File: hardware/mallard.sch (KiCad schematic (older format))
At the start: 84 parts, among them J1 USB_A, J2 Conn_02x03_Odd_Even, J3 Conn_01x03, J4 Conn_01x03, J5 Conn_01x03, J6 Conn_01x03, SW1 RESET Switch, U1 TMP235, U10 LTC1983ES6-3, U11 STM32L4Q5xx, U12 LTC3529EDCB, U2 TMP235, U3 TMP235, U4 BQ24210DQCT, U5 TMUX1309, U6 TMUX1309, U7 LMP7721, U8 TPS71710DRVR, U9 LMV554

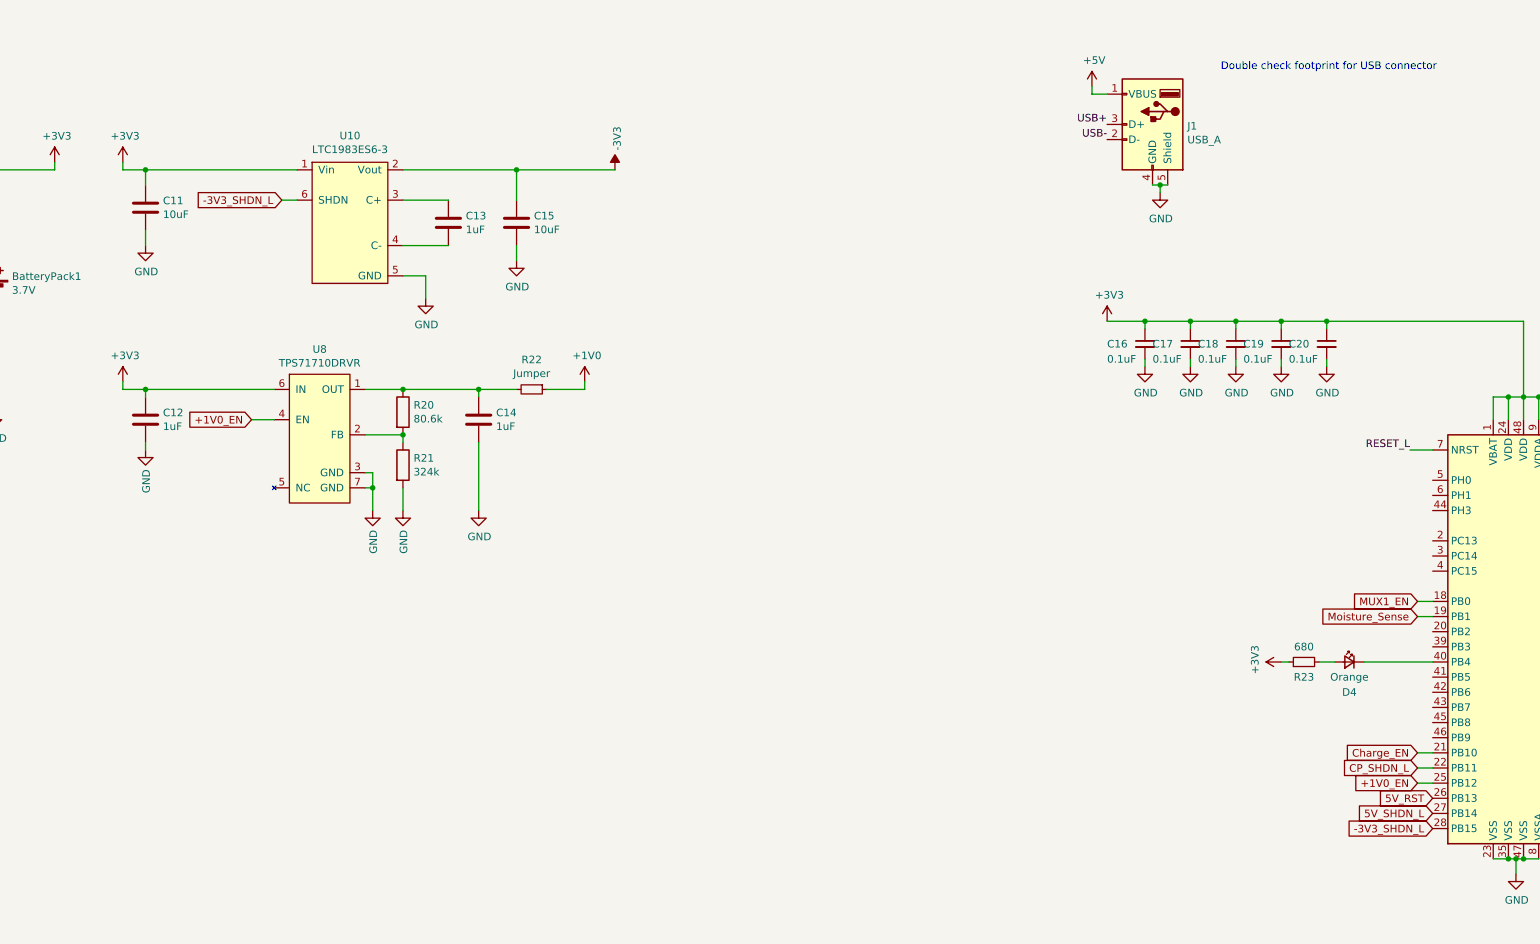
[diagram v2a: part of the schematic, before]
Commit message: Replaced -3V charge pump with LM828
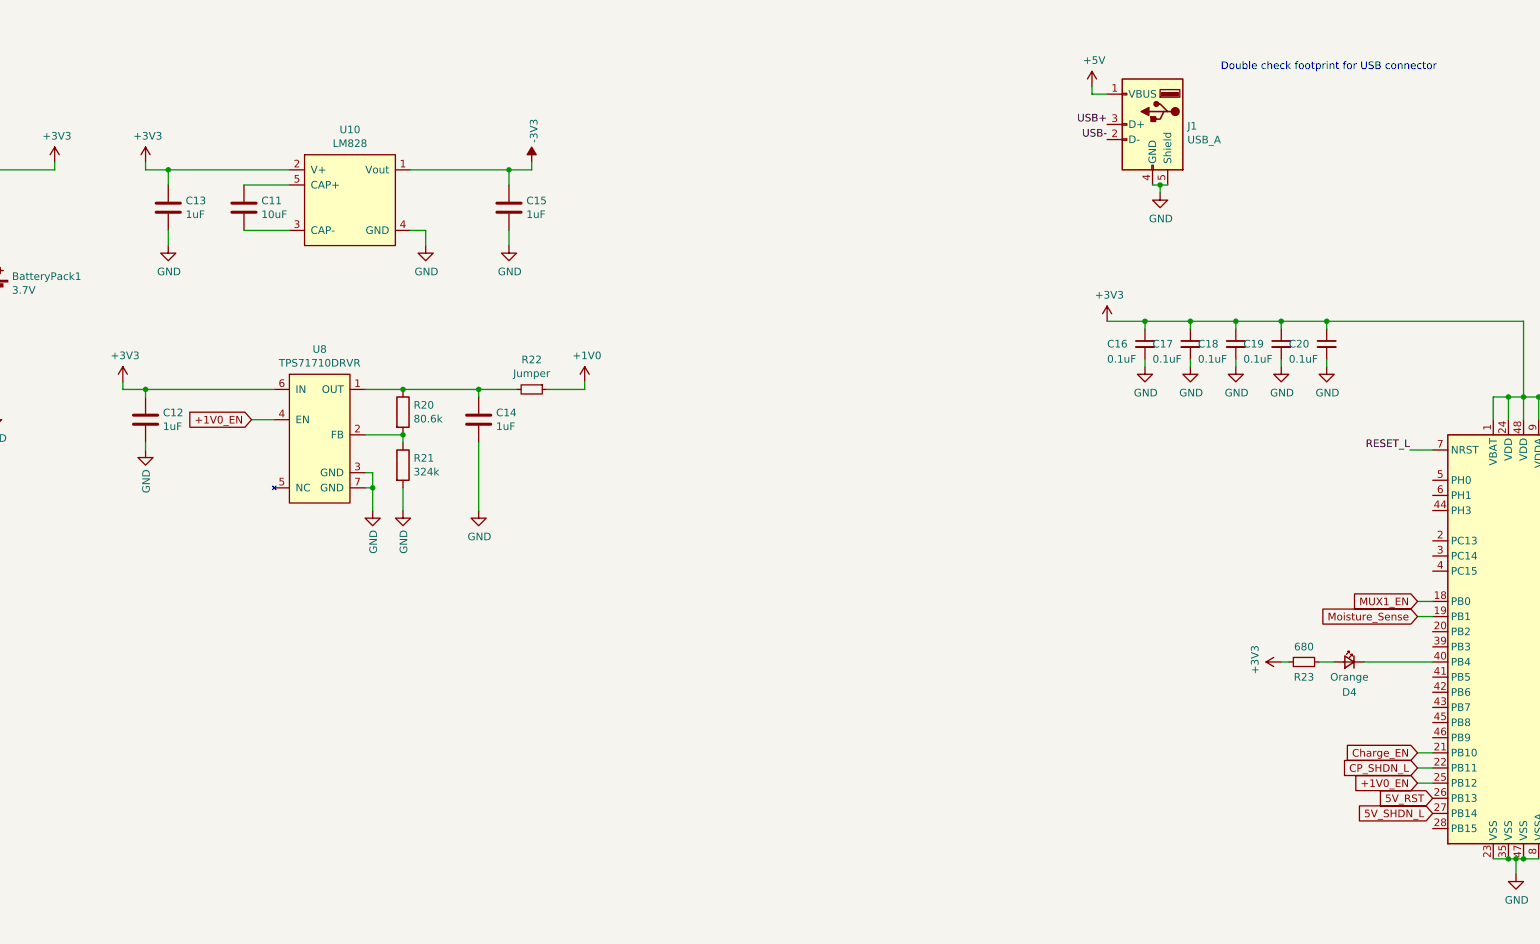
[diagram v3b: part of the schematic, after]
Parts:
- removed U10: LTC1983ES6-3, Package_TO_SOT_SMD:SOT-23-6, symbol mallard-rescue:LTC1983ES6-3-mallard
- added U10: LM828, Package_TO_SOT_SMD:SOT-23-5, symbol mallard:LM828
- C13: Digikey 1276-1019-1-ND -> 311-1446-1-ND
- C15: value 10uF -> 1uF; Digikey 587-3258-1-ND -> 311-1446-1-ND
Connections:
- net +3V3: now also C13.1, U10.2 (V+); no longer C11.1
- net -3V3: now also U10.1 (Vout)
- net GND: now also C13.2, U10.4 (GND); no longer C11.2
- net -3V3_SHDN_L: no longer names the net of U11.28 (PB15)
- new net: C11.2, U10.3 (CAP-)
- new net: C11.1, U10.5 (CAP+)
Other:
- moved on the sheet: C11
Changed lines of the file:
@@
 	1700 10800 1700 10900
-Wire Wire Line
-	9650 3200 9950 3200
-Wire Wire Line
-	9650 3500 9950 3500
 Wire Wire Line
 	3050 3950 2950 3950
@@
 F 3 "" H 2450 4600 50  0001 C CNN
 	1    2450 4600
-	1    0    0    -1
-$EndComp
-$Comp
-L mallard-rescue:GND-power #PWR0149
-U 1 1 62037076
-P 9800 3850
-F 0 "#PWR0149" H 9800 3600 50  0001 C CNN
-F 1 "GND" H 9805 3677 50  0000 C CNN
-F 2 "" H 9800 3850 50  0001 C CNN
-F 3 "" H 9800 3850 50  0001 C CNN
-	1    9800 3850
 	1    0    0    -1
 $EndComp
@@
 Wire Wire Line
 	6950 3000 7350 3000
-$Comp
-L mallard-rescue:GND-power #PWR0154
-U 1 1 620370B8
-P 7950 3500
-F 0 "#PWR0154" H 7950 3250 50  0001 C CNN
-F 1 "GND" H 7955 3327 50  0000 C CNN
-F 2 "" H 7950 3500 50  0001 C CNN
-F 3 "" H 7950 3500 50  0001 C CNN
-	1    7950 3500
-	1    0    0    -1
-$EndComp
-Wire Wire Line
-	7950 3400 7950 3500
 Wire Wire Line
 	1450 3000 1000 3000
@@
 L mallard-rescue:C-Device C11
 U 1 1 620370D8
-P 7950 3250
-F 0 "C11" H 8065 3296 50  0000 L CNN
-F 1 "10uF" H 8065 3205 50  0000 L CNN
-F 2 "Capacitor_SMD:C_0603_1608Metric_Pad1.08x0.95mm_HandSolder" H 7988 3100 50  0001 C CNN
-F 3 "https://www.yuden.co.jp/productdata/catalog/mlcc06_e.pdf" H 7950 3250 50  0001 C CNN
-F 4 "587-3258-1-ND" H 7950 3250 50  0001 C CNN "Digikey"
-	1    7950 3250
-	1    0    0    -1
-$EndComp
-$Comp
-L mallard-rescue:C-Device C13
-U 1 1 620370DF
-P 9950 3350
-F 0 "C13" H 10065 3396 50  0000 L CNN
-F 1 "1uF" H 10065 3305 50  0000 L CNN
-F 2 "Capacitor_SMD:C_0603_1608Metric_Pad1.08x0.95mm_HandSolder" H 9988 3200 50  0001 C CNN
-F 3 "http://weblib.samsungsem.com/mlcc/mlcc-ec-data-sheet.do?partNumber=CL10B105KO8NNN" H 9950 3350 50  0001 C CNN
-F 4 "1276-1019-1-ND" H 9950 3350 50  0001 C CNN "Digikey"
-	1    9950 3350
+P 8600 3250
+F 0 "C11" H 8715 3296 50  0000 L CNN
+F 1 "10uF" H 8715 3205 50  0000 L CNN
+F 2 "Capacitor_SMD:C_0603_1608Metric_Pad1.08x0.95mm_HandSolder" H 8638 3100 50  0001 C CNN
+F 3 "https://www.yuden.co.jp/productdata/catalog/mlcc06_e.pdf" H 8600 3250 50  0001 C CNN
+F 4 "587-3258-1-ND" H 8600 3250 50  0001 C CNN "Digikey"
+	1    8600 3250
 	1    0    0    -1
 $EndComp
@@
 F 4 "296-28738-1-ND" H 3550 2900 50  0001 C CNN "Digikey"
 	1    3550 2900
-	1    0    0    -1
-$EndComp
-$Comp
-L mallard-rescue:LTC1983ES6-3-mallard U10
-U 1 1 620370FA
-P 9300 2900
-F 0 "U10" H 9300 3025 50  0000 C CNN
-F 1 "LTC1983ES6-3" H 9300 2934 50  0000 C CNN
-F 2 "Package_TO_SOT_SMD:SOT-23-6" H 9300 1850 50  0001 C CNN
-F 3 "https://www.analog.com/media/en/technical-documentation/data-sheets/1983fc.pdf" H 9300 2900 50  0001 C CNN
-F 4 "LTC1983ES6-3#TRPBFCT-ND" H 9300 2900 50  0001 C CNN "Digikey"
-	1    9300 2900
 	1    0    0    -1
 $EndComp
@@
 	-1   0    0    1
 $EndComp
-Text GLabel 8850 3200 0    50   Input ~ 0
--3V3_SHDN_L
-Wire Wire Line
-	8950 3200 8850 3200
-$Comp
-L mallard-rescue:-3V3-power #PWR0156
-U 1 1 62037111
-P 11050 3000
-F 0 "#PWR0156" H 11050 3100 50  0001 C CNN
-F 1 "-3V3" V 11065 3128 50  0000 L CNN
-F 2 "" H 11050 3000 50  0001 C CNN
-F 3 "" H 11050 3000 50  0001 C CNN
-	1    11050 3000
-	1    0    0    -1
-$EndComp
 $Comp
 L mallard-rescue:GND-power #PWR0157
@@
 Wire Wire Line
 	7350 3000 7350 2950
-$Comp
-L mallard-rescue:+3V3-power #PWR0162
-U 1 1 6203717F
-P 7800 2950
-F 0 "#PWR0162" H 7800 2800 50  0001 C CNN
-F 1 "+3V3" H 7815 3123 50  0000 C CNN
-F 2 "" H 7800 2950 50  0001 C CNN
-F 3 "" H 7800 2950 50  0001 C CNN
-	1    7800 2950
-	1    0    0    -1
-$EndComp
-Wire Wire Line
-	7950 3000 7950 3100
-Wire Wire Line
-	7950 3000 8950 3000
-Wire Wire Line
-	7950 3000 7800 3000
-Wire Wire Line
-	7800 3000 7800 2950
-Connection ~ 7950 3000
-Wire Wire Line
-	9650 3000 10400 3000
-$Comp
-L mallard-rescue:GND-power #PWR0163
-U 1 1 6203718B
-P 10400 3600
-F 0 "#PWR0163" H 10400 3350 50  0001 C CNN
-F 1 "GND" H 10405 3427 50  0000 C CNN
-F 2 "" H 10400 3600 50  0001 C CNN
-F 3 "" H 10400 3600 50  0001 C CNN
-	1    10400 3600
-	1    0    0    -1
-$EndComp
-Wire Wire Line
-	10400 3500 10400 3600
-$Comp
-L mallard-rescue:C-Device C15
-U 1 1 62037193
-P 10400 3350
-F 0 "C15" H 10515 3396 50  0000 L CNN
-F 1 "10uF" H 10515 3305 50  0000 L CNN
-F 2 "Capacitor_SMD:C_0603_1608Metric_Pad1.08x0.95mm_HandSolder" H 10438 3200 50  0001 C CNN
-F 3 "https://www.yuden.co.jp/productdata/catalog/mlcc06_e.pdf" H 10400 3350 50  0001 C CNN
-F 4 "587-3258-1-ND" H 10400 3350 50  0001 C CNN "Digikey"
-	1    10400 3350
-	1    0    0    -1
-$EndComp
-Wire Wire Line
-	10400 3000 10400 3200
-Connection ~ 10400 3000
-Wire Wire Line
-	10400 3000 11050 3000
-Wire Wire Line
-	9650 3700 9800 3700
-Wire Wire Line
-	9800 3700 9800 3850
 $Comp
 L mallard-rescue:C-Device C4
@@
 Text GLabel 16450 7150 0    50   Input ~ 0
 5V_RST
-Text GLabel 16450 7350 0    50   Input ~ 0
--3V3_SHDN_L
 Wire Wire Line
 	3200 6300 3600 6300
@@
 	3200 6650 3600 6650
 Connection ~ 3600 6650
+$Comp
+L mallard:LM828 U10
+U 1 1 61F55449
+P 9300 2850
+F 0 "U10" H 9300 2965 50  0000 C CNN
+F 1 "LM828" H 9300 2874 50  0000 C CNN
+F 2 "Package_TO_SOT_SMD:SOT-23-5" H 9300 2000 50  0001 C CNN
+F 3 "https://www.ti.com/lit/ds/symlink/lm828.pdf?HQS=dis-dk-null-digikeymode-dsf-pf-null-wwe&ts=1643222784613&ref_url=https%253A%252F%252Fwww.ti.com%252Fgeneral%252Fdocs%252Fsuppproductinfo.tsp%253FdistId%253D10%2526gotoUrl%253Dhttps%253A%252F%252Fwww.ti.com%252Flit%252Fgpn%252Flm828" H 9300 2850 50  0001 C CNN
+F 4 "296-36289-1-ND" H 9300 2100 50  0001 C CNN "Digikey"
+	1    9300 2850
+	1    0    0    -1
+$EndComp
+Wire Wire Line
+	8600 3100 8900 3100
+Wire Wire Line
+	8600 3400 8900 3400
+Connection ~ 8100 3000
+Wire Wire Line
+	8100 3000 8900 3000
+Wire Wire Line
+	7950 3000 7950 2950
+Wire Wire Line
+	8100 3000 7950 3000
+Wire Wire Line
+	8100 3000 8100 3100
+$Comp
+L mallard-rescue:+3V3-power #PWR0162
+U 1 1 6203717F
+P 7950 2950
+F 0 "#PWR0162" H 7950 2800 50  0001 C CNN
+F 1 "+3V3" H 7965 3123 50  0000 C CNN
+F 2 "" H 7950 2950 50  0001 C CNN
+F 3 "" H 7950 2950 50  0001 C CNN
+	1    7950 2950
+	1    0    0    -1
+$EndComp
+Wire Wire Line
+	8100 3400 8100 3500
+$Comp
+L mallard-rescue:GND-power #PWR0154
+U 1 1 620370B8
+P 8100 3500
+F 0 "#PWR0154" H 8100 3250 50  0001 C CNN
+F 1 "GND" H 8105 3327 50  0000 C CNN
+F 2 "" H 8100 3500 50  0001 C CNN
+F 3 "" H 8100 3500 50  0001 C CNN
+	1    8100 3500
+	1    0    0    -1
+$EndComp
+Wire Wire Line
+	10350 3000 10350 3100
+Wire Wire Line
+	10350 3400 10350 3500
+$Comp
+L mallard-rescue:GND-power #PWR0149
+U 1 1 62090527
+P 10350 3500
+F 0 "#PWR0149" H 10350 3250 50  0001 C CNN
+F 1 "GND" H 10355 3327 50  0000 C CNN
+F 2 "" H 10350 3500 50  0001 C CNN
+F 3 "" H 10350 3500 50  0001 C CNN
+	1    10350 3500
+	1    0    0    -1
+$EndComp
+Wire Wire Line
+	9700 3000 10350 3000
+Connection ~ 10350 3000
+Wire Wire Line
+	10350 3000 10500 3000
+$Comp
+L mallard-rescue:GND-power #PWR0156
+U 1 1 620C8C7F
+P 9800 3500
+F 0 "#PWR0156" H 9800 3250 50  0001 C CNN
+F 1 "GND" H 9805 3327 50  0000 C CNN
+F 2 "" H 9800 3500 50  0001 C CNN
+F 3 "" H 9800 3500 50  0001 C CNN
+	1    9800 3500
+	1    0    0    -1
+$EndComp
+Wire Wire Line
+	9700 3400 9800 3400
+Wire Wire Line
+	9800 3400 9800 3500
+$Comp
+L mallard-rescue:-3V3-power #PWR0163
+U 1 1 6211D80B
+P 10500 2950
+F 0 "#PWR0163" H 10500 3050 50  0001 C CNN
+F 1 "-3V3" V 10515 3078 50  0000 L CNN
+F 2 "" H 10500 2950 50  0001 C CNN
+F 3 "" H 10500 2950 50  0001 C CNN
+	1    10500 2950
+	1    0    0    -1
+$EndComp
+Wire Wire Line
+	10500 3000 10500 2950
+$Comp
+L mallard-rescue:C-Device C13
+U 1 1 62191547
+P 8100 3250
+F 0 "C13" H 8215 3296 50  0000 L CNN
+F 1 "1uF" H 8215 3205 50  0000 L CNN
+F 2 "Capacitor_SMD:C_0603_1608Metric_Pad1.08x0.95mm_HandSolder" H 8138 3100 50  0001 C CNN
+F 3 "https://www.yageo.com/upload/media/product/productsearch/datasheet/mlcc/UPY-GPHC_X7R_6.3V-to-50V_20.pdf" H 8100 3250 50  0001 C CNN
+F 4 "311-1446-1-ND" H 8100 3250 50  0001 C CNN "Digikey"
+	1    8100 3250
+	1    0    0    -1
+$EndComp
+$Comp
+L mallard-rescue:C-Device C15
+U 1 1 621ABDE8
+P 10350 3250
+F 0 "C15" H 10465 3296 50  0000 L CNN
+F 1 "1uF" H 10465 3205 50  0000 L CNN
+F 2 "Capacitor_SMD:C_0603_1608Metric_Pad1.08x0.95mm_HandSolder" H 10388 3100 50  0001 C CNN
+F 3 "https://www.yageo.com/upload/media/product/productsearch/datasheet/mlcc/UPY-GPHC_X7R_6.3V-to-50V_20.pdf" H 10350 3250 50  0001 C CNN
+F 4 "311-1446-1-ND" H 10350 3250 50  0001 C CNN "Digikey"
+	1    10350 3250
+	1    0    0    -1
+$EndComp
 $EndSCHEMATC

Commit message: Updated temperature sensor PN
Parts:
- U1, U2, U3: Digikey 296-48860-1-ND -> 296-TMP235AEDBZTQ1CT-ND
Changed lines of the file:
@@
 F 1 "TMP235" H -5100 12534 50  0000 C CNN
 F 2 "" H -5100 12000 50  0001 C CNN
-F 3 "https://www.ti.com/lit/ds/symlink/tmp235.pdf?HQS=dis-dk-null-digikeymode-dsf-pf-null-wwe&ts=1626470161926&ref_url=https%253A%252F%252Fwww.ti.com%252Fgeneral%252Fdocs%252Fsuppproductinfo.tsp%253FdistId%253D10%2526gotoUrl%253Dhttps%253A%252F%252Fwww.ti.com%252Flit%252Fgpn%252Ftmp235" H -5100 12000 50  0001 C CNN
-F 4 "296-48860-1-ND" H -5100 12450 50  0001 C CNN "Digikey"
+F 3 "https://www.ti.com/lit/ds/symlink/tmp235-q1.pdf?HQS=dis-dk-null-digikeymode-dsf-pf-null-wwe&ts=1643211475158&ref_url=https%253A%252F%252Fwww.ti.com%252Fgeneral%252Fdocs%252Fsuppproductinfo.tsp%253FdistId%253D10%2526gotoUrl%253Dhttps%253A%252F%252Fwww.ti.com%252Flit%252Fgpn%252Ftmp235-q1" H -5100 12000 50  0001 C CNN
+F 4 "296-TMP235AEDBZTQ1CT-ND" H -5100 12450 50  0001 C CNN "Digikey"
 	1    -5100 12450
 	1    0    0    -1
@@
 F 2 "" H -5100 12900 50  0001 C CNN
 F 3 "https://www.ti.com/lit/ds/symlink/tmp235.pdf?HQS=dis-dk-null-digikeymode-dsf-pf-null-wwe&ts=1626470161926&ref_url=https%253A%252F%252Fwww.ti.com%252Fgeneral%252Fdocs%252Fsuppproductinfo.tsp%253FdistId%253D10%2526gotoUrl%253Dhttps%253A%252F%252Fwww.ti.com%252Flit%252Fgpn%252Ftmp235" H -5100 12900 50  0001 C CNN
-F 4 "296-48860-1-ND" H -5100 13350 50  0001 C CNN "Digikey"
+F 4 "296-TMP235AEDBZTQ1CT-ND" H -5100 13350 50  0001 C CNN "Digikey"
 	1    -5100 13350
 	1    0    0    -1
@@
 F 2 "" H -5150 13750 50  0001 C CNN
 F 3 "https://www.ti.com/lit/ds/symlink/tmp235.pdf?HQS=dis-dk-null-digikeymode-dsf-pf-null-wwe&ts=1626470161926&ref_url=https%253A%252F%252Fwww.ti.com%252Fgeneral%252Fdocs%252Fsuppproductinfo.tsp%253FdistId%253D10%2526gotoUrl%253Dhttps%253A%252F%252Fwww.ti.com%252Flit%252Fgpn%252Ftmp235" H -5150 13750 50  0001 C CNN
-F 4 "296-48860-1-ND" H -5150 14200 50  0001 C CNN "Digikey"
+F 4 "296-TMP235AEDBZTQ1CT-ND" H -5150 14200 50  0001 C CNN "Digikey"
 	1    -5150 14200
 	1    0    0    -1
